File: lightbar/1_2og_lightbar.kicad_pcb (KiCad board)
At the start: 2 copper layers, 61.7 x 18.6 mm, 35 parts, among them J1 Conn_01x03

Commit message: spacing updates, silkscreens and etc
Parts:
- J1: footprint Connector_Molex:Molex_Pico-EZmate_78171-0003_1x03-1MP_P1.20mm_Vertical -> Connector_PinHeader_2.54mm:PinHeader_1x03_P2.54mm_Vertical
- moved J1 5.73 mm to (27.1, 33.5), turned to -90 degrees
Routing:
- net +5V: track 96.5 -> 105.0 mm, vias 17 -> 16
- net LIGHTBAR_RGB_OUT: track 8.65 -> 13.5 mm
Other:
- outline, holes or cut-outs redrawn
- board text added: "5V"
- board text added: "D"
- board text added: "G"

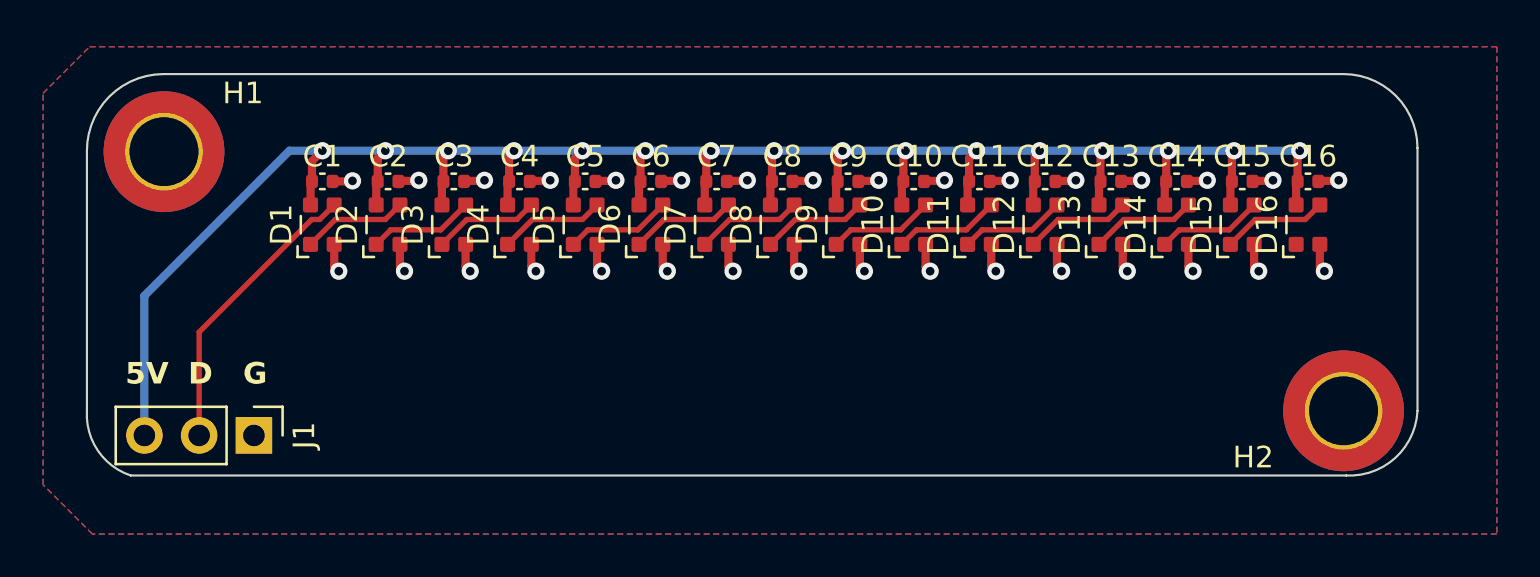
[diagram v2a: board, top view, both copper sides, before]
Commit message: update gerbers, change mounting hole dimensions
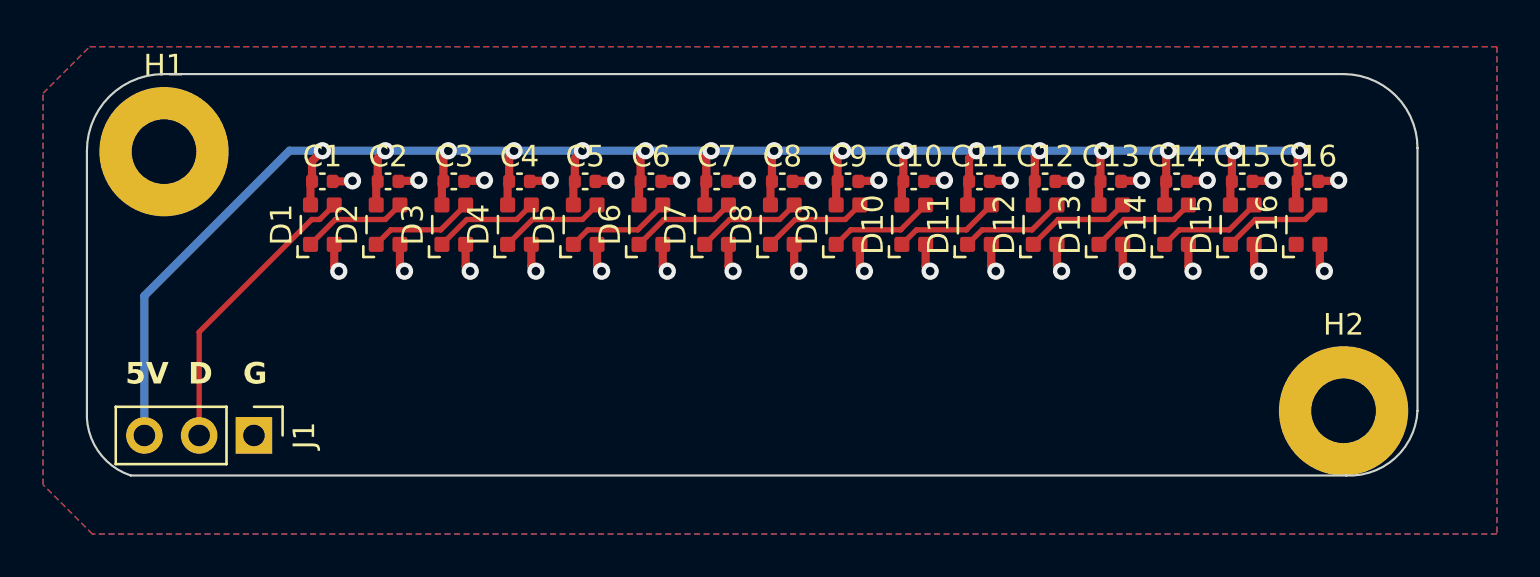
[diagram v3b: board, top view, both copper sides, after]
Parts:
- H1, H2: footprint MountingHole:MountingHole_3.2mm_M3_DIN965_Pad_TopBottom -> MountingHole:MountingHole_3mm_Pad
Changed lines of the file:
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@@
     )
   )
-  (footprint "MountingHole:MountingHole_3.2mm_M3_DIN965_Pad_TopBottom" (layer "F.Cu")
+  (footprint "MountingHole:MountingHole_3mm_Pad" (layer "F.Cu")
     (at 77.597 32.385)
-    (descr "Mounting Hole 3.2mm, M3, DIN965")
-    (tags "mounting hole 3.2mm m3 din965")
+    (descr "Mounting Hole 3mm")
+    (tags "mounting hole 3mm")
     (property "Sheetfile" "1_2og_lightbar.kicad_sch")
     (property "Sheetname" "")
     (property "ki_description" "Mounting Hole with connection")
     (property "ki_keywords" "mounting hole")
-    (attr exclude_from_pos_files exclude_from_bom)
-    (fp_text reference "H2" (at -4.191 2.159) (layer "F.SilkS")
-        (effects (font (size 1 1) (thickness 0.15)))
-    )
-    (fp_text value "MountingHole_Pad" (at 0 3.8) (layer "F.Fab")
-        (effects (font (size 1 1) (thickness 0.15)))
-    )
-    (fp_text user "${REFERENCE}" (at 0 0) (layer "F.Fab")
-        (effects (font (size 1 1) (thickness 0.15)))
-    )
-    (fp_circle (center 0 0) (end 2.8 0)
+    (attr exclude_from_pos_files)
+    (fp_text reference "H2" (at 0 -4) (layer "F.SilkS")
+        (effects (font (size 1 1) (thickness 0.15)))
+    )
+    (fp_text value "MountingHole_Pad" (at 0 4) (layer "F.Fab")
+        (effects (font (size 1 1) (thickness 0.15)))
+    )
+    (fp_text user "${REFERENCE}" (at 0 0) (layer "F.Fab")
+        (effects (font (size 1 1) (thickness 0.15)))
+    )
+    (fp_circle (center 0 0) (end 3 0)
       (stroke (width 0.15) (type solid)) (fill none) (layer "Cmts.User"))
-    (fp_circle (center 0 0) (end 3.05 0)
+    (fp_circle (center 0 0) (end 3.25 0)
       (stroke (width 0.05) (type solid)) (fill none) (layer "F.CrtYd"))
-    (pad "1" thru_hole circle (at 0 0) (size 3.6 3.6) (drill 3.2) (layers "*.Cu" "*.Mask")
-      (net 2 "GND") (pinfunction "1") (pintype "input"))
-    (pad "1" connect circle (at 0 0) (size 5.6 5.6) (layers "F.Cu" "F.Mask")
-      (net 2 "GND") (pinfunction "1") (pintype "input"))
-    (pad "1" connect circle (at 0 0) (size 5.6 5.6) (layers "B.Cu" "B.Mask")
+    (pad "1" thru_hole circle (at 0 0) (size 6 6) (drill 3) (layers "*.Cu" "*.Mask")
       (net 2 "GND") (pinfunction "1") (pintype "input"))
   )
@@
     (property "Sheetfile" "1_2og_lightbar.kicad_sch")
     (property "Sheetname" "")
-    (property "ki_description" "Generic connectable mounting pin connector, single row, 01x03, script generated (kicad-library-utils/schlib/autogen/connector/)")
+    (property "ki_description" "Generic connector, single row, 01x03, script generated (kicad-library-utils/schlib/autogen/connector/)")
     (property "ki_keywords" "connector")
     (attr through_hole)
@@
     )
   )
-  (footprint "MountingHole:MountingHole_3.2mm_M3_DIN965_Pad_TopBottom" (layer "F.Cu")
+  (footprint "MountingHole:MountingHole_3mm_Pad" (layer "F.Cu")
     (at 22.879961 20.362871)
-    (descr "Mounting Hole 3.2mm, M3, DIN965")
-    (tags "mounting hole 3.2mm m3 din965")
+    (descr "Mounting Hole 3mm")
+    (tags "mounting hole 3mm")
     (property "Sheetfile" "1_2og_lightbar.kicad_sch")
     (property "Sheetname" "")
     (property "ki_description" "Mounting Hole with connection")
     (property "ki_keywords" "mounting hole")
-    (attr exclude_from_pos_files exclude_from_bom)
-    (fp_text reference "H1" (at 3.663039 -2.709871) (layer "F.SilkS")
-        (effects (font (size 1 1) (thickness 0.15)))
-    )
-    (fp_text value "MountingHole_Pad" (at 0 3.8) (layer "F.Fab")
-        (effects (font (size 1 1) (thickness 0.15)))
-    )
-    (fp_text user "${REFERENCE}" (at 0 0) (layer "F.Fab")
-        (effects (font (size 1 1) (thickness 0.15)))
-    )
-    (fp_circle (center 0 0) (end 2.8 0)
+    (attr exclude_from_pos_files)
+    (fp_text reference "H1" (at 0 -4) (layer "F.SilkS")
+        (effects (font (size 1 1) (thickness 0.15)))
+    )
+    (fp_text value "MountingHole_Pad" (at 0 4) (layer "F.Fab")
+        (effects (font (size 1 1) (thickness 0.15)))
+    )
+    (fp_text user "${REFERENCE}" (at 0 0) (layer "F.Fab")
+        (effects (font (size 1 1) (thickness 0.15)))
+    )
+    (fp_circle (center 0 0) (end 3 0)
       (stroke (width 0.15) (type solid)) (fill none) (layer "Cmts.User"))
-    (fp_circle (center 0 0) (end 3.05 0)
+    (fp_circle (center 0 0) (end 3.25 0)
       (stroke (width 0.05) (type solid)) (fill none) (layer "F.CrtYd"))
-    (pad "1" thru_hole circle (at 0 0) (size 3.6 3.6) (drill 3.2) (layers "*.Cu" "*.Mask")
+    (pad "1" thru_hole circle (at 0 0) (size 6 6) (drill 3) (layers "*.Cu" "*.Mask")
       (net 2 "GND") (pinfunction "1") (pintype "input"))
-    (pad "1" connect circle (at 0 0) (size 5.6 5.6) (layers "F.Cu" "F.Mask")
-      (net 2 "GND") (pinfunction "1") (pintype "input"))
-    (pad "1" connect circle (at 0 0) (size 5.6 5.6) (layers "B.Cu" "B.Mask")
-      (net 2 "GND") (pinfunction "1") (pintype "input"))
-  )
+  )

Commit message: idk
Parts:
- added J2: Conn_01x03_Shielded, Connector_Molex:Molex_Pico-EZmate_78171-0003_1x03-1MP_P1.20mm_Vertical, F.Cu at (24.5, 32.5)
- added R1: 500, Resistor_SMD:R_0805_2012Metric, F.Cu at (27.0, 23.4)
- added R2: 500, Resistor_SMD:R_0805_2012Metric, F.Cu at (78.5, 22.5)
- D1, D10, D11, D12, D13, D14, D15, D16, D2, D3, D4, D5, D6, D7, D8, D9: value WS2812_2020 -> SK6812_EC15; footprint marbastlib-various:LED_WS2812_2020 -> LED_SMD:LED_SK6812_EC15_1.5x1.5mm
- moved J1 7.65 mm to (22.0, 27.8), turned to 90 degrees
- moved C13 2.56 mm to (65.6, 24.0), turned to 180 degrees
- moved C11 2.56 mm to (59.5, 24.0), turned to 180 degrees
- moved C3 2.56 mm to (35.1, 24.0), turned to 180 degrees
- moved C7 2.56 mm to (47.3, 24.0), turned to 180 degrees
- moved C1 2.56 mm to (29.0, 24.0), turned to 180 degrees
- moved C10 2.56 mm to (56.5, 24.0), turned to 180 degrees
- moved C12 2.56 mm to (62.6, 24.0), turned to 180 degrees
- moved C14 2.56 mm to (68.7, 24.0), turned to 180 degrees
- moved C15 2.56 mm to (71.7, 24.0), turned to 180 degrees
- moved C16 2.56 mm to (74.8, 24.0), turned to 180 degrees
- moved C2 2.56 mm to (32.1, 24.0), turned to 180 degrees
- moved C4 2.56 mm to (38.2, 24.0), turned to 180 degrees
- moved C5 2.56 mm to (41.2, 24.0), turned to 180 degrees
- moved C6 2.56 mm to (44.3, 24.0), turned to 180 degrees
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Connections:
- D1 pad 3: LIGHTBAR_RGB_OUT -> Net-(D1-DIN)
- D16 pad 1: unconnected-(D16-DOUT-Pad1) -> Net-(D16-DOUT)
- J1 pad 1: GND -> +5V
- J1 pad 3: +5V -> GND
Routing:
- net GND: track 35.6 -> 65.5 mm, vias 32 -> 15
- net +5V: track 105.0 -> 113.0 mm
- net LIGHTBAR_RGB_OUT: track 13.5 -> 7.45 mm
- net Net-(D16-DOUT): track 0.00 -> 3.29 mm
- net Net-(D3-DOUT): track 4.91 -> 2.52 mm
- net Net-(D13-DOUT): track 4.91 -> 2.52 mm
- net Net-(D11-DOUT): track 4.91 -> 2.52 mm
- net Net-(D7-DOUT): track 4.91 -> 2.52 mm
- net Net-(D4-DOUT): track 4.91 -> 2.52 mm
- net Net-(D14-DOUT): track 4.91 -> 2.52 mm
- net Net-(D12-DOUT): track 4.91 -> 2.52 mm
- net Net-(D1-DOUT): track 4.91 -> 2.52 mm
- net Net-(D8-DOUT): track 4.91 -> 2.52 mm
- net Net-(D6-DOUT): track 4.91 -> 2.52 mm
- net Net-(D2-DOUT): track 4.91 -> 2.52 mm
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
